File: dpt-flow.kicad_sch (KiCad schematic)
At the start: 50 parts, among them J29 FLOW, J30 FLOW, J31 FLOW, J32 FLOW, J33 FLOW, J34 FLOW, J35 FLOW, J36 FLOW, J37 FLOW, J38 FLOW, J39 FLOW, J40 FLOW, J5 PT UPW 1, J6 PT HFE 1, J7 PT UPW 2, J8 PT HFE 2, U56 LTC4316CMS, U57 LTC4316CMS, U58 LTC4316CMS, U59 LTC4316CMS

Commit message: 540 COMPONENTS I AM LOSING MY MINDDDDDD
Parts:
- renumbered C104 to C120, C105 to C121, C106 to C122, C107 to C123, C119 to C124, C123 to C125, C129 to C127, C122 to C128, C125 to C129, C121 to C130, C124 to C131, C127 to C132, C130 to C133, C128 to C134, C131 to C135, J5 to J25, J6 to J26, J7 to J27, J8 to J28, J32 to J30, J35 to J31, J38 to J32, J31 to J33, J30 to J35, J33 to J36, J36 to J37, J39 to J38, J37 to J39, R237 to R198, R238 to R199, R239 to R200, R240 to R201, R241 to R202, R242 to R203, R243 to R204, R244 to R205, R245 to R206, R246 to R207, R247 to R208, R248 to R209, R249 to R210, R250 to R211, U59 to U100, U56 to U97, U57 to U98, U58 to U99

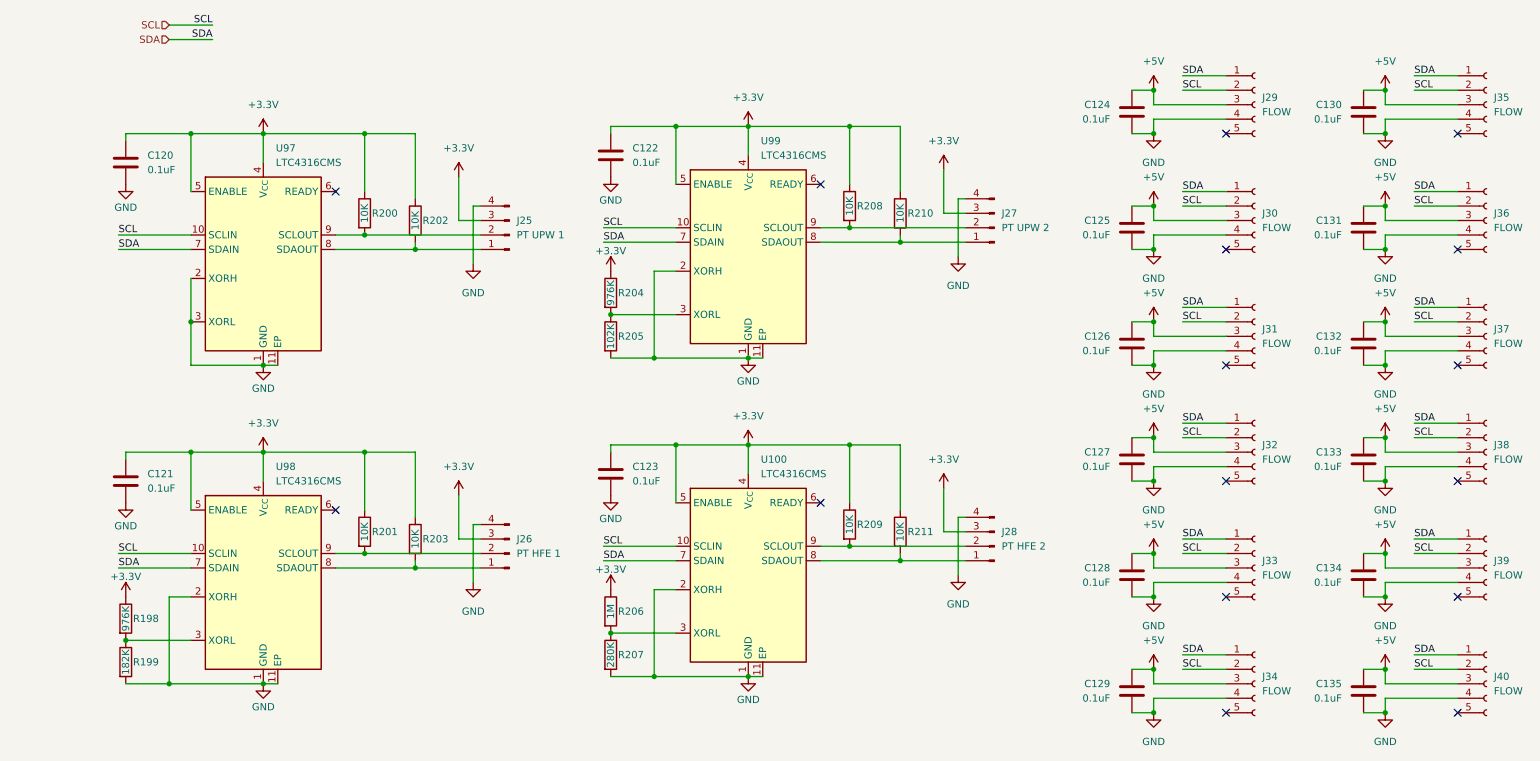
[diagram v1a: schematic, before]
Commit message: page sizes
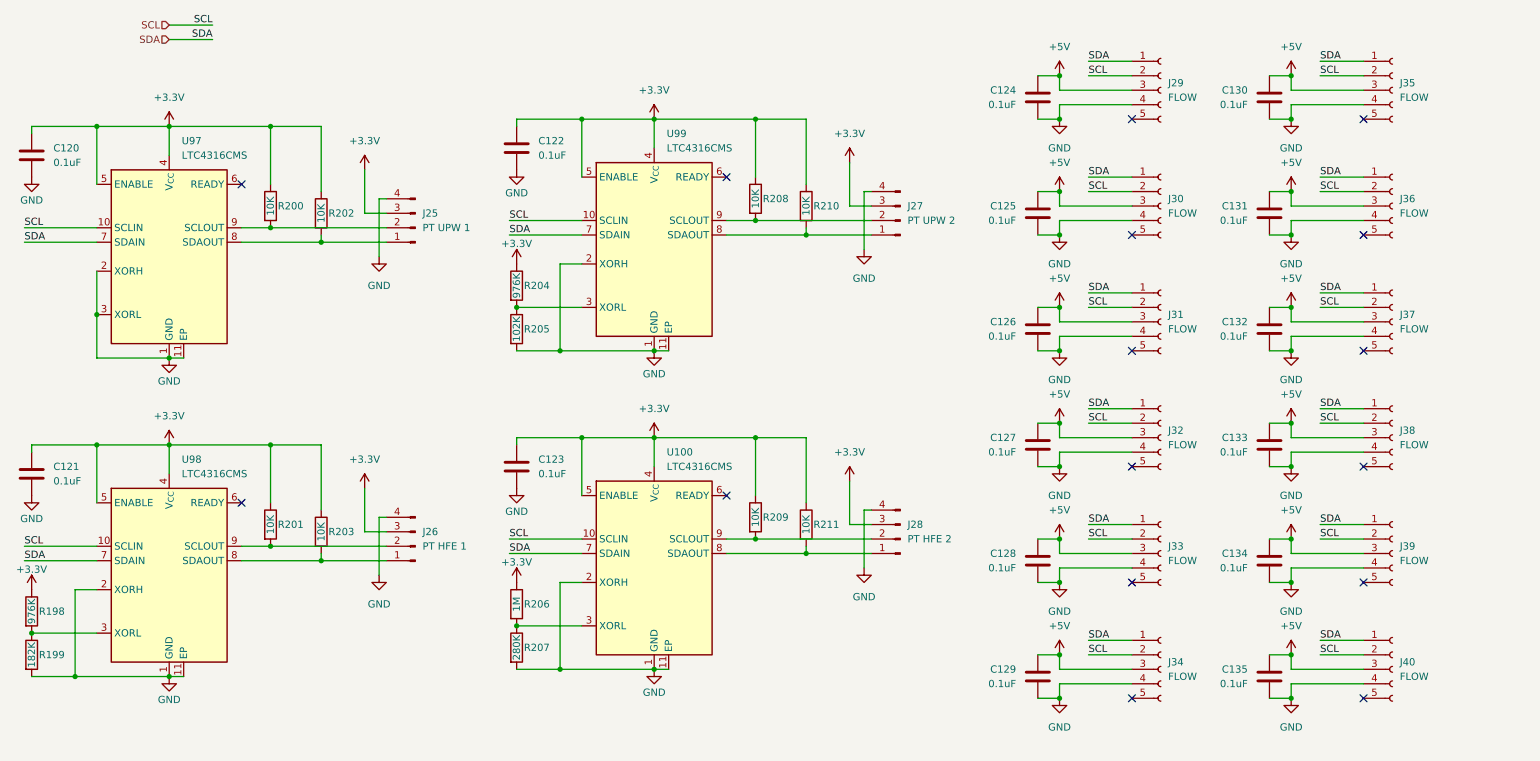
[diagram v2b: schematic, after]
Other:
- moved on the sheet: C120, C121, C122, C123, C124, C125, C126, C127, C128, C129, C130, C131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

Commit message: schematic finished milestone
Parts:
- renumbered C120 to C139, C121 to C140, C122 to C141, C123 to C142, C124 to C143, C125 to C144, C126 to C145, C127 to C146, C128 to C147, C129 to C148, C130 to C149, C131 to C150, C132 to C151, C133 to C152, C134 to C153, C135 to C154, R198 to R207, R199 to R208, R200 to R209, R201 to R210, R202 to R211, R203 to R212, R204 to R213, R205 to R214, R206 to R215, R207 to R216, R208 to R217, R209 to R218, R210 to R219, R211 to R220

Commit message: capacitor footprints
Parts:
- C139, C140, C141, C142, C143, C144, C145, C146, C147, C148, C149, C150, C151, C152, C153, C154: footprint (none) -> Capacitor_SMD:C_0603_1608Metric
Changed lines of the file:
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@@
 			)
 		)
-		(property "Footprint" ""
+		(property "Footprint" "Capacitor_SMD:C_0603_1608Metric"
 			(at 192.0748 100.33 0)
 			(effects
@@
 			)
 		)
-		(property "Footprint" ""
+		(property "Footprint" "Capacitor_SMD:C_0603_1608Metric"
 			(at 232.7148 120.65 0)
 			(effects
@@
 			)
 		)
-		(property "Footprint" ""
+		(property "Footprint" "Capacitor_SMD:C_0603_1608Metric"
 			(at 232.7148 140.97 0)
 			(effects
@@
 			)
 		)
-		(property "Footprint" ""
+		(property "Footprint" "Capacitor_SMD:C_0603_1608Metric"
 			(at 102.5652 104.14 0)
 			(effects
@@
 			)
 		)
-		(property "Footprint" ""
+		(property "Footprint" "Capacitor_SMD:C_0603_1608Metric"
 			(at 102.5652 48.26 0)
 			(effects
@@
 			)
 		)
-		(property "Footprint" ""
+		(property "Footprint" "Capacitor_SMD:C_0603_1608Metric"
 			(at 17.4752 49.53 0)
 			(effects
@@
 			)
 		)
-		(property "Footprint" ""
+		(property "Footprint" "Capacitor_SMD:C_0603_1608Metric"
 			(at 192.0748 59.69 0)
 			(effects
@@
 			)
 		)
-		(property "Footprint" ""
+		(property "Footprint" "Capacitor_SMD:C_0603_1608Metric"
 			(at 192.0748 39.37 0)
 			(effects
@@
 			)
 		)
-		(property "Footprint" ""
+		(property "Footprint" "Capacitor_SMD:C_0603_1608Metric"
 			(at 17.4752 105.41 0)
 			(effects
@@
 			)
 		)
-		(property "Footprint" ""
+		(property "Footprint" "Capacitor_SMD:C_0603_1608Metric"
 			(at 232.7148 100.33 0)
 			(effects
@@
 			)
 		)
-		(property "Footprint" ""
+		(property "Footprint" "Capacitor_SMD:C_0603_1608Metric"
 			(at 192.0748 140.97 0)
 			(effects
@@
 			)
 		)
-		(property "Footprint" ""
+		(property "Footprint" "Capacitor_SMD:C_0603_1608Metric"
 			(at 192.0748 120.65 0)
 			(effects
@@
 			)
 		)
-		(property "Footprint" ""
+		(property "Footprint" "Capacitor_SMD:C_0603_1608Metric"
 			(at 232.7148 39.37 0)
 			(effects
@@
 			)
 		)
-		(property "Footprint" ""
+		(property "Footprint" "Capacitor_SMD:C_0603_1608Metric"
 			(at 232.7148 59.69 0)
 			(effects
@@
 			)
 		)
-		(property "Footprint" ""
+		(property "Footprint" "Capacitor_SMD:C_0603_1608Metric"
 			(at 232.7148 80.01 0)
 			(effects
@@
 			)
 		)
-		(property "Footprint" ""
+		(property "Footprint" "Capacitor_SMD:C_0603_1608Metric"
 			(at 192.0748 80.01 0)
 			(effects

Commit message: add more footprints
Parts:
- R207, R208, R209, R210, R211, R212, R213, R214, R215, R216, R217, R218, R219, R220: footprint (none) -> Resistor_SMD:R_0603_1608Metric
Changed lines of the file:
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@@
 			)
 		)
-		(property "Footprint" ""
+		(property "Footprint" "Resistor_SMD:R_0603_1608Metric"
 			(at 150.622 110.49 90)
 			(effects
@@
 			)
 		)
-		(property "Footprint" ""
+		(property "Footprint" "Resistor_SMD:R_0603_1608Metric"
 			(at 56.642 110.49 90)
 			(effects
@@
 			)
 		)
-		(property "Footprint" ""
+		(property "Footprint" "Resistor_SMD:R_0603_1608Metric"
 			(at 99.822 124.46 90)
 			(effects
@@
 			)
 		)
-		(property "Footprint" ""
+		(property "Footprint" "Resistor_SMD:R_0603_1608Metric"
 			(at 99.822 132.08 90)
 			(effects
@@
 			)
 		)
-		(property "Footprint" ""
+		(property "Footprint" "Resistor_SMD:R_0603_1608Metric"
 			(at 141.732 53.34 90)
 			(effects
@@
 			)
 		)
-		(property "Footprint" ""
+		(property "Footprint" "Resistor_SMD:R_0603_1608Metric"
 			(at 65.532 55.88 90)
 			(effects
@@
 			)
 		)
-		(property "Footprint" ""
+		(property "Footprint" "Resistor_SMD:R_0603_1608Metric"
 			(at 99.822 76.2 90)
 			(effects
@@
 			)
 		)
-		(property "Footprint" ""
+		(property "Footprint" "Resistor_SMD:R_0603_1608Metric"
 			(at 56.642 54.61 90)
 			(effects
@@
 			)
 		)
-		(property "Footprint" ""
+		(property "Footprint" "Resistor_SMD:R_0603_1608Metric"
 			(at 99.822 68.58 90)
 			(effects
@@
 			)
 		)
-		(property "Footprint" ""
+		(property "Footprint" "Resistor_SMD:R_0603_1608Metric"
 			(at 141.732 109.22 90)
 			(effects
@@
 			)
 		)
-		(property "Footprint" ""
+		(property "Footprint" "Resistor_SMD:R_0603_1608Metric"
 			(at 65.532 111.76 90)
 			(effects
@@
 			)
 		)
-		(property "Footprint" ""
+		(property "Footprint" "Resistor_SMD:R_0603_1608Metric"
 			(at 14.732 133.35 90)
 			(effects
@@
 			)
 		)
-		(property "Footprint" ""
+		(property "Footprint" "Resistor_SMD:R_0603_1608Metric"
 			(at 14.732 125.73 90)
 			(effects
@@
 			)
 		)
-		(property "Footprint" ""
+		(property "Footprint" "Resistor_SMD:R_0603_1608Metric"
 			(at 150.622 54.61 90)
 			(effects
